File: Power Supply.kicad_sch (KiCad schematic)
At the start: 22 parts, among them U2 MPQ4436GRE-AEC1-P, U3 RT9080-33GJ5

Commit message: Assigning footprints
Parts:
- C1, C1D1, C2, C3, C4, C5, C6: footprint (none) -> Capacitor_SMD:C_0603_1608Metric
- C1A1, C1B1, C2A1, C2B1: footprint (none) -> Capacitor_SMD:C_1206_3216Metric
- C1C1: value 10u -> 0.1u; footprint (none) -> Capacitor_SMD:C_0603_1608Metric
- R1, R3, R4, R5, R6, R7: footprint (none) -> Resistor_SMD:R_0603_1608Metric
- U2: footprint QFN-4x4_MPQ4436-AEC1_MNP -> MPQ4436GRE-AEC1-Z:QFN-4x4_MPQ4436-AEC1_MNP
- U3: footprint TSOT-23-5_RIT -> RT9080_33GJ5:TSOT-23-5_RIT
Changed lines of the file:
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@@
       (effects (font (size 1.524 1.524)))
     )
-    (property "Footprint" "TSOT-23-5_RIT" (at 128.27 123.19 0)
+    (property "Footprint" "RT9080_33GJ5:TSOT-23-5_RIT" (at 128.27 123.19 0)
       (effects (font (size 1.27 1.27) italic) hide)
     )
@@
       (effects (font (size 1.27 1.27)) (justify right))
     )
-    (property "Footprint" "" (at 232.7148 92.71 0)
+    (property "Footprint" "Capacitor_SMD:C_1206_3216Metric" (at 232.7148 92.71 0)
       (effects (font (size 1.27 1.27)) hide)
     )
@@
       (effects (font (size 1.27 1.27)) (justify left))
     )
-    (property "Footprint" "" (at 110.7948 95.25 0)
+    (property "Footprint" "Capacitor_SMD:C_0603_1608Metric" (at 110.7948 95.25 0)
       (effects (font (size 1.27 1.27)) hide)
     )
@@
       (effects (font (size 1.27 1.27)) (justify left))
     )
-    (property "Footprint" "" (at 80.3148 95.25 0)
+    (property "Footprint" "Capacitor_SMD:C_1206_3216Metric" (at 80.3148 95.25 0)
       (effects (font (size 1.27 1.27)) hide)
     )
@@
       (effects (font (size 1.27 1.27)) (justify left))
     )
-    (property "Footprint" "" (at 177.4952 133.35 0)
+    (property "Footprint" "Capacitor_SMD:C_0603_1608Metric" (at 177.4952 133.35 0)
       (effects (font (size 1.27 1.27)) hide)
     )
@@
       (effects (font (size 1.27 1.27)) (justify left))
     )
-    (property "Footprint" "" (at 54.3052 76.2 0)
+    (property "Footprint" "Capacitor_SMD:C_0603_1608Metric" (at 54.3052 76.2 0)
       (effects (font (size 1.27 1.27)) hide)
     )
@@
       (effects (font (size 1.27 1.27)) (justify left))
     )
-    (property "Footprint" "" (at 117.1448 133.35 0)
+    (property "Footprint" "Capacitor_SMD:C_0603_1608Metric" (at 117.1448 133.35 0)
       (effects (font (size 1.27 1.27)) hide)
     )
@@
       (effects (font (size 1.27 1.27)) (justify left))
     )
-    (property "Footprint" "" (at 212.344 100.584 90)
+    (property "Footprint" "Resistor_SMD:R_0603_1608Metric" (at 212.344 100.584 90)
       (effects (font (size 1.27 1.27)) hide)
     )
@@
       (effects (font (size 1.27 1.27)))
     )
-    (property "Footprint" "" (at 181.356 73.406 90)
+    (property "Footprint" "Resistor_SMD:R_0603_1608Metric" (at 181.356 73.406 90)
       (effects (font (size 1.27 1.27)) hide)
     )
@@
       (effects (font (size 1.27 1.27)) (justify left))
     )
-    (property "Footprint" "" (at 221.2848 92.71 0)
+    (property "Footprint" "Capacitor_SMD:C_0603_1608Metric" (at 221.2848 92.71 0)
       (effects (font (size 1.27 1.27)) hide)
     )
@@
       (effects (font (size 1.524 1.524)))
     )
-    (property "Footprint" "QFN-4x4_MPQ4436-AEC1_MNP" (at 171.45 64.77 0)
+    (property "Footprint" "MPQ4436GRE-AEC1-Z:QFN-4x4_MPQ4436-AEC1_MNP" (at 171.45 64.77 0)
       (effects (font (size 1.27 1.27) italic) hide)
     )
@@
       (effects (font (size 1.27 1.27)) (justify left))
     )
-    (property "Value" "10u" (at 99.06 92.71 0)
-      (effects (font (size 1.27 1.27)) (justify left))
-    )
-    (property "Footprint" "" (at 100.6348 95.25 0)
+    (property "Value" "0.1u" (at 99.06 92.71 0)
+      (effects (font (size 1.27 1.27)) (justify left))
+    )
+    (property "Footprint" "Capacitor_SMD:C_0603_1608Metric" (at 100.6348 95.25 0)
       (effects (font (size 1.27 1.27)) hide)
     )
@@
       (effects (font (size 1.27 1.27)) (justify left))
     )
-    (property "Footprint" "" (at 212.344 89.154 90)
+    (property "Footprint" "Resistor_SMD:R_0603_1608Metric" (at 212.344 89.154 90)
       (effects (font (size 1.27 1.27)) hide)
     )
@@
       (effects (font (size 1.27 1.27)) (justify left))
     )
-    (property "Footprint" "" (at 242.8748 92.71 0)
+    (property "Footprint" "Capacitor_SMD:C_1206_3216Metric" (at 242.8748 92.71 0)
       (effects (font (size 1.27 1.27)) hide)
     )
@@
       (effects (font (size 1.27 1.27)) (justify right))
     )
-    (property "Footprint" "" (at 185.7248 73.66 0)
+    (property "Footprint" "Capacitor_SMD:C_0603_1608Metric" (at 185.7248 73.66 0)
       (effects (font (size 1.27 1.27)) hide)
     )
@@
       (effects (font (size 1.27 1.27)))
     )
-    (property "Footprint" "" (at 181.864 86.106 90)
+    (property "Footprint" "Resistor_SMD:R_0603_1608Metric" (at 181.864 86.106 90)
       (effects (font (size 1.27 1.27)) hide)
     )
@@
       (effects (font (size 1.27 1.27)) (justify left))
     )
-    (property "Footprint" "" (at 90.4748 95.25 0)
+    (property "Footprint" "Capacitor_SMD:C_1206_3216Metric" (at 90.4748 95.25 0)
       (effects (font (size 1.27 1.27)) hide)
     )
@@
       (effects (font (size 1.27 1.27)) (justify left))
     )
-    (property "Footprint" "" (at 66.294 89.154 90)
+    (property "Footprint" "Resistor_SMD:R_0603_1608Metric" (at 66.294 89.154 90)
       (effects (font (size 1.27 1.27)) hide)
     )
@@
       (effects (font (size 1.27 1.27)) (justify left))
     )
-    (property "Footprint" "" (at 68.2752 102.87 0)
+    (property "Footprint" "Capacitor_SMD:C_0603_1608Metric" (at 68.2752 102.87 0)
       (effects (font (size 1.27 1.27)) hide)
     )
@@
       (effects (font (size 1.27 1.27)) (justify left))
     )
-    (property "Footprint" "" (at 45.974 71.374 90)
-      (effects (font (size 1.27 1.27)) hide)
-    )
+    (property "Footprint" "Resistor_SMD:R_0603_1608Metric" (at 45.974 71.374 90)
+      (effects (font (size 1.27 1.27)) hide)
+    )

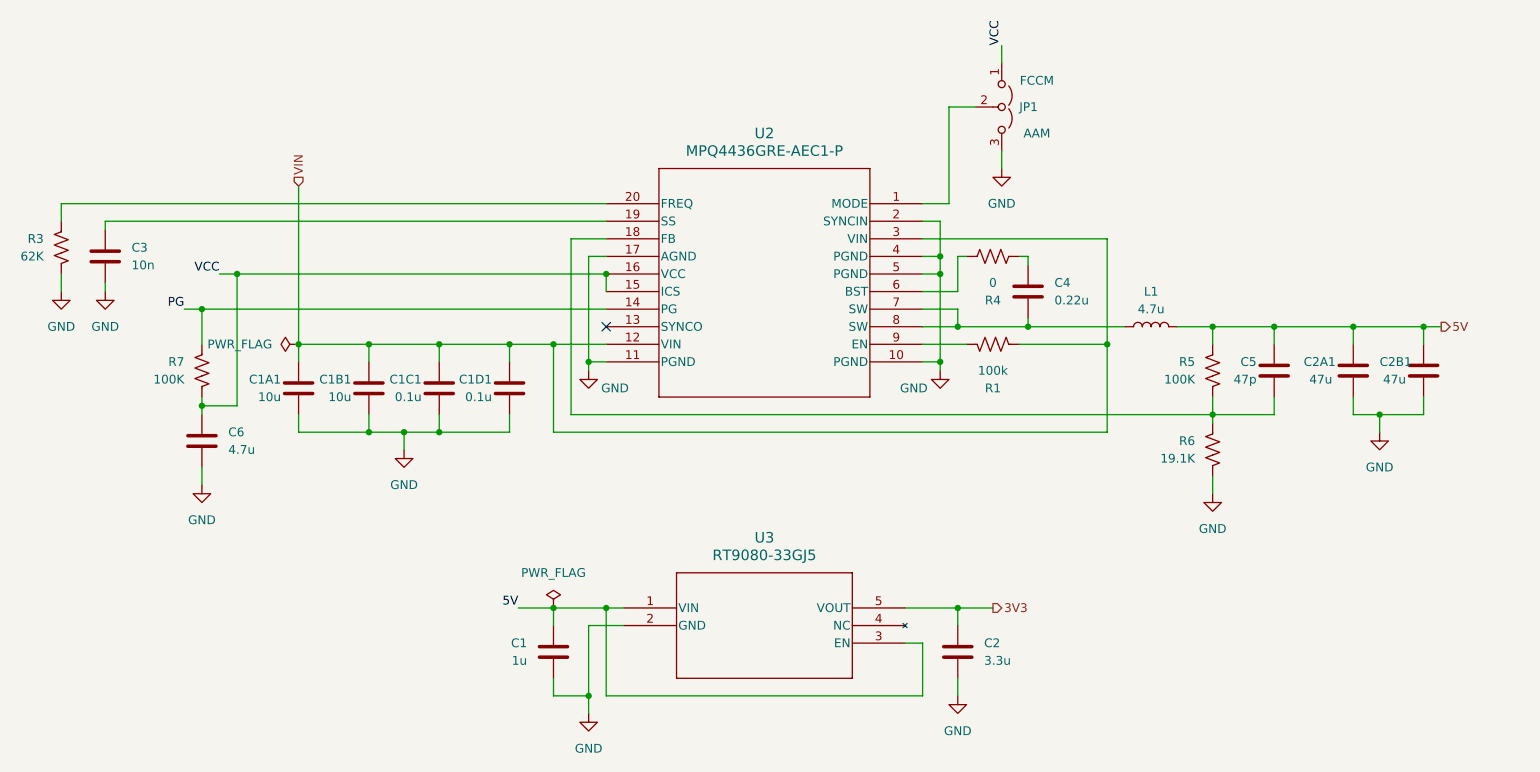
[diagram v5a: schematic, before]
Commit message: finished assigning footprints and started PCB layout
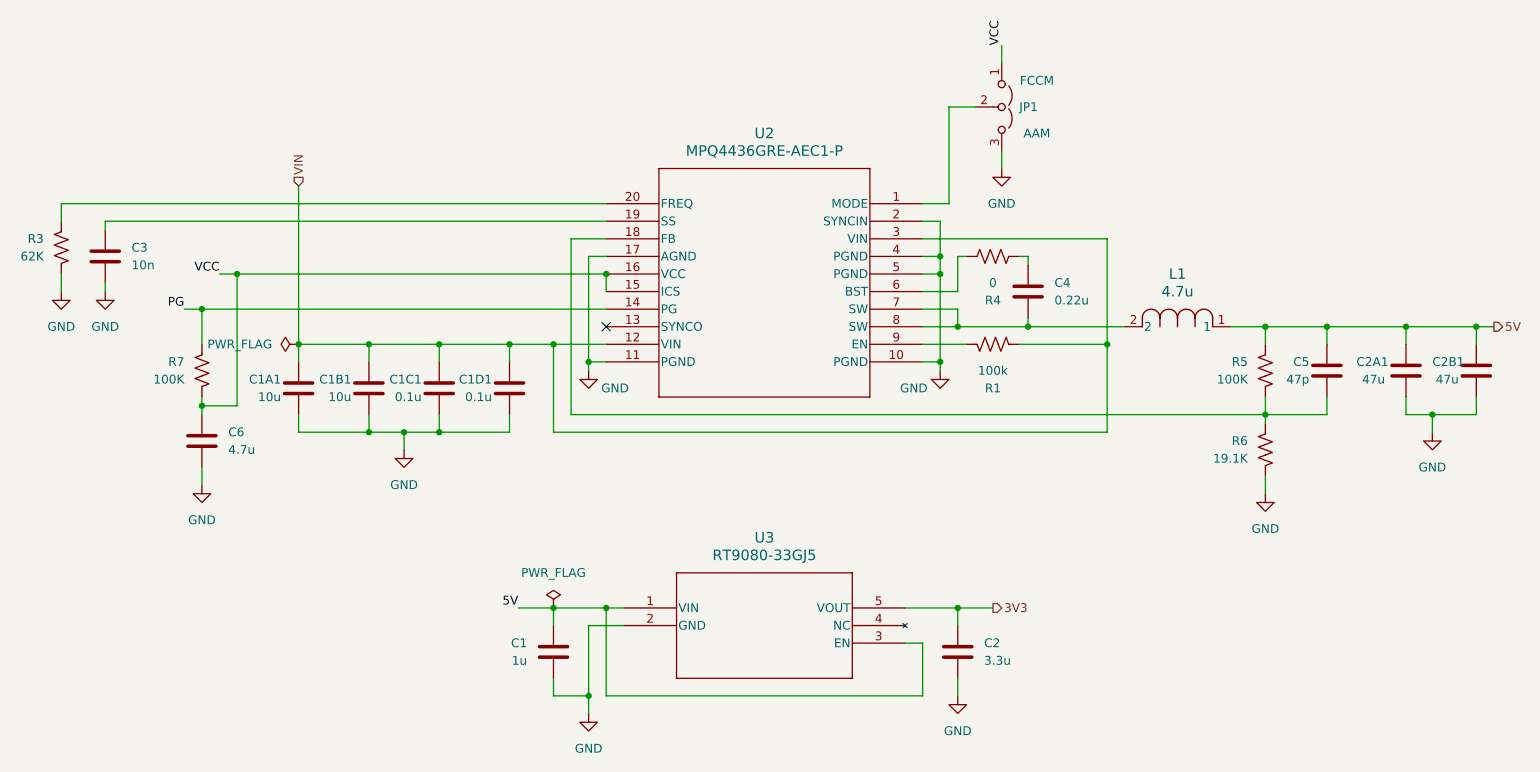
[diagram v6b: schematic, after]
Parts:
- removed L1: 4.7u, symbol Device:L
- added L1: 4.7u, IND_PA4342_PUL, symbol PA4342_472NLT:PA4342.472NLT
- JP1: footprint (none) -> Connector_PinHeader_2.54mm:PinHeader_1x03_P2.54mm_Vertical
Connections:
- net 5V: now also L1.1
- net at C4.1, U2.7 (SW), U2.8 (SW): now also L1.2
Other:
- moved on the sheet: C2A1, C2B1, C5, R5, R6

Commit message: add LED for debugging
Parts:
- L1: footprint IND_PA4342_PUL -> PA4342_472NLT:IND_PA4342_PUL
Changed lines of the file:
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@@
       (effects (font (size 1.524 1.524)))
     )
-    (property "Footprint" "IND_PA4342_PUL" (at 200.66 82.55 0)
+    (property "Footprint" "PA4342_472NLT:IND_PA4342_PUL" (at 200.66 82.55 0)
       (effects (font (size 1.27 1.27) italic) hide)
     )
